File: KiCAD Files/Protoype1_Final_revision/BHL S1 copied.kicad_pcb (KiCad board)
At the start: 4 copper layers, 64 x 64 mm, 108 parts, among them IC1 NUP2105LT1G, IC2 NUP2105LT1G, IC3 IR2136STRPBF, J1 Conn_01x03_Pin, J2 Conn_01x03_Pin, J3 Conn_01x03_Pin, Q1 CSD19502Q5B, Q2 CSD19502Q5B, Q3 CSD19502Q5B, Q4 CSD19502Q5B, Q5 CSD19502Q5B, Q7 CSD19502Q5B, U1 ME6211C30M5, U2 SPX3819M5-L-5-0, U3 Solder Pad, U4 STM32G431CBU6, U5 STM32G431CBU6, Y1 8MHz, Y2 8MHz

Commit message: unlocked files
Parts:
- removed U4: STM32G431CBU6, Footprint for BHL S1:STM32G431CBU6_MCU
- moved R35 3.58 mm to (148.6, 72.8)
- moved R37 3.58 mm to (148.6, 74.5)
- moved Y1 3.58 mm to (144.2, 74.5)
- moved C27 3.56 mm to (134.8, 63.7)
- moved C31 3.56 mm to (134.8, 65.7)
- moved C32 3.56 mm to (134.8, 67.7)
- moved C34 3.56 mm to (134.8, 69.6)
- moved C35 3.56 mm to (134.8, 71.6)
- moved C36 3.56 mm to (134.8, 73.6)
- moved R1 3.56 mm to (138.1, 75.9)
- moved R38 3.56 mm to (138.6, 73.7)
- moved J3 3.56 mm to (138.7, 65.0)
- moved U5 1.94 mm to (145.8, 65.8)

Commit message: Fixed GND Net label issue on PCB creation
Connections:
- AS5600 pad 4: Curr_fdbk1_OPAmp- -> GND
- C1 pad 2: Curr_fdbk1_OPAmp- -> GND
- C11 pad 2: Curr_fdbk1_OPAmp- -> GND
- C12 pad 2: Curr_fdbk1_OPAmp- -> GND
- C14 pad 2: Curr_fdbk1_OPAmp- -> GND
- C16 pad 1: Curr_fdbk1_OPAmp- -> GND
- C18 pad 2: Curr_fdbk1_OPAmp- -> GND
- C2 pad 2: Curr_fdbk1_OPAmp- -> GND
- C22 pad 2: Curr_fdbk1_OPAmp- -> GND
- C23 pad 2: Curr_fdbk1_OPAmp- -> GND
- C24 pad 2: Curr_fdbk1_OPAmp- -> GND
- C25 pad 2: Curr_fdbk1_OPAmp- -> GND
- C26 pad 2: Curr_fdbk1_OPAmp- -> GND
- C27 pad 2: Curr_fdbk1_OPAmp- -> GND
- C28 pad 2: Curr_fdbk1_OPAmp- -> GND
- C29 pad 2: Curr_fdbk1_OPAmp- -> GND
- C3 pad 2: Curr_fdbk1_OPAmp- -> GND
- C30 pad 2: Curr_fdbk1_OPAmp- -> GND
- C31 pad 2: Curr_fdbk1_OPAmp- -> GND
- C32 pad 2: Curr_fdbk1_OPAmp- -> GND
- C33 pad 2: Curr_fdbk1_OPAmp- -> GND
- C34 pad 2: Curr_fdbk1_OPAmp- -> GND
- C35 pad 1: Curr_fdbk1_OPAmp- -> GND
- C36 pad 2: Curr_fdbk1_OPAmp- -> GND
- C4 pad 2: Curr_fdbk1_OPAmp- -> GND
- D1 pad 1: Curr_fdbk1_OPAmp- -> GND
- D2 pad 2: Curr_fdbk1_OPAmp- -> GND
- Header2X2H1 pad 2: Curr_fdbk1_OPAmp- -> GND
- Header2X2H2 pad 2: Curr_fdbk1_OPAmp- -> GND
- IC1 pad 3: Curr_fdbk1_OPAmp- -> GND
- IC2 pad 3: Curr_fdbk1_OPAmp- -> GND
- IC3 pad 10: Curr_fdbk1_OPAmp- -> GND
- IC3 pad 13: Curr_fdbk1_OPAmp- -> GND
- J2 pad 2: Curr_fdbk1_OPAmp- -> GND
- J3 pad 2: Curr_fdbk1_OPAmp- -> GND
- R11 pad 1: Curr_fdbk1_OPAmp- -> GND
- R16 pad 1: Curr_fdbk1_OPAmp- -> GND
- R17 pad 1: Curr_fdbk1_OPAmp- -> GND
- R20 pad 2: Curr_fdbk1_OPAmp- -> GND
- R23 pad 1: Curr_fdbk1_OPAmp- -> GND
- R26 pad 2: Curr_fdbk1_OPAmp- -> GND
- R30 pad 1: Curr_fdbk1_OPAmp- -> GND
- R30 pad 2: Curr_fdbk1_OPAmp- -> GND
- R32 pad 1: Curr_fdbk1_OPAmp- -> GND
- R36 pad 1: Curr_fdbk1_OPAmp- -> GND
- R8 pad 1: Curr_fdbk1_OPAmp- -> GND
- S1 pad 1: Curr_fdbk1_OPAmp- -> GND
- S1 pad 2: Curr_fdbk1_OPAmp- -> GND
- TCAN1051HGVDR1 pad 2: Curr_fdbk1_OPAmp- -> GND
- TCAN1051HGVDR1 pad 8: Curr_fdbk1_OPAmp- -> GND
- U1 pad 2: Curr_fdbk1_OPAmp- -> GND
- U2 pad 2: Curr_fdbk1_OPAmp- -> GND
- U5 pad 11: Curr_fdbk1_OPAmp- -> GND
- U5 pad 13: Curr_fdbk1_OPAmp- -> GND
- U5 pad 19: Curr_fdbk1_OPAmp- -> GND
- U5 pad 49: Curr_fdbk1_OPAmp- -> GND
- Y1 pad 3: Curr_fdbk1_OPAmp- -> GND
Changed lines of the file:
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@@
 			(layers "F.Cu" "F.Mask" "F.Paste")
 			(roundrect_rratio 0.25)
-			(net 20 "Curr_fdbk1_OPAmp-")
+			(net 5 "GND")
 			(pintype "passive")
 		)
@@
 			(layers "F.Cu" "F.Mask" "F.Paste")
 			(roundrect_rratio 0.212766)
-			(net 20 "Curr_fdbk1_OPAmp-")
+			(net 5 "GND")
 			(pintype "passive")
 		)
@@
 			(layers "F.Cu" "F.Mask" "F.Paste")
 			(roundrect_rratio 0.25)
-			(net 20 "Curr_fdbk1_OPAmp-")
+			(net 5 "GND")
 			(pintype "passive")
 		)
@@
 			(layers "F.Cu" "F.Mask" "F.Paste")
 			(roundrect_rratio 0.25)
-			(net 20 "Curr_fdbk1_OPAmp-")
+			(net 5 "GND")
 			(pintype "passive")
 		)
@@
 			(layers "F.Cu" "F.Mask" "F.Paste")
 			(roundrect_rratio 0.25)
-			(net 20 "Curr_fdbk1_OPAmp-")
+			(net 5 "GND")
 			(pintype "passive")
 		)
@@
 			(size 2 4.1)
 			(layers "F.Cu" "F.Mask" "F.Paste")
-			(net 20 "Curr_fdbk1_OPAmp-")
+			(net 5 "GND")
 			(pintype "passive")
 		)
@@
 			(layers "*.Cu" "*.Mask")
 			(remove_unused_layers no)
-			(net 20 "Curr_fdbk1_OPAmp-")
+			(net 5 "GND")
 			(pinfunction "Pin_2")
 			(pintype "passive")
@@
 			(layers "F.Cu" "F.Mask" "F.Paste")
 			(roundrect_rratio 0.25)
-			(net 20 "Curr_fdbk1_OPAmp-")
+			(net 5 "GND")
 			(pintype "passive")
 		)
@@
 			(layers "F.Cu" "F.Mask" "F.Paste")
 			(roundrect_rratio 0.25)
-			(net 20 "Curr_fdbk1_OPAmp-")
+			(net 5 "GND")
 			(pinfunction "V_{SS}")
 			(pintype "power_in")
@@
 			(layers "F.Cu" "F.Mask" "F.Paste")
 			(roundrect_rratio 0.25)
-			(net 20 "Curr_fdbk1_OPAmp-")
+			(net 5 "GND")
 			(pintype "passive")
 		)
@@
 			(layers "F.Cu" "F.Mask" "F.Paste")
 			(roundrect_rratio 0.212766)
-			(net 20 "Curr_fdbk1_OPAmp-")
+			(net 5 "GND")
 			(pintype "passive")
 		)
@@
 			(layers "F.Cu" "F.Mask" "F.Paste")
 			(roundrect_rratio 0.25)
-			(net 20 "Curr_fdbk1_OPAmp-")
+			(net 5 "GND")
 			(pintype "passive")
 		)
@@
 			(layers "F.Cu" "F.Mask" "F.Paste")
 			(roundrect_rratio 0.25)
-			(net 20 "Curr_fdbk1_OPAmp-")
+			(net 5 "GND")
 			(pinfunction "K")
 			(pintype "passive")
@@
 			(layers "F.Cu" "F.Mask" "F.Paste")
 			(roundrect_rratio 0.25)
-			(net 20 "Curr_fdbk1_OPAmp-")
+			(net 5 "GND")
 			(pintype "passive")
 		)
@@
 			(layers "F.Cu" "F.Mask" "F.Paste")
 			(roundrect_rratio 0.25)
-			(net 20 "Curr_fdbk1_OPAmp-")
+			(net 5 "GND")
 			(pinfunction "A")
 			(pintype "passive")
@@
 			(layers "F.Cu" "F.Mask" "F.Paste")
 			(roundrect_rratio 0.25)
-			(net 20 "Curr_fdbk1_OPAmp-")
+			(net 5 "GND")
 			(pintype "passive")
 		)
@@
 			(layers "F.Cu" "F.Mask" "F.Paste")
 			(roundrect_rratio 0.25)
-			(net 20 "Curr_fdbk1_OPAmp-")
+			(net 5 "GND")
 			(pintype "passive")
 		)
@@
 			(layers "F.Cu" "F.Mask" "F.Paste")
 			(roundrect_rratio 0.212766)
-			(net 20 "Curr_fdbk1_OPAmp-")
+			(net 5 "GND")
 			(pintype "passive")
 		)
@@
 			(layers "F.Cu" "F.Mask" "F.Paste")
 			(roundrect_rratio 0.25)
-			(net 20 "Curr_fdbk1_OPAmp-")
+			(net 5 "GND")
 			(pintype "passive")
 		)
@@
 			(layers "F.Cu" "F.Mask" "F.Paste")
 			(roundrect_rratio 0.25)
-			(net 20 "Curr_fdbk1_OPAmp-")
+			(net 5 "GND")
 			(pintype "passive")
 		)
@@
 			(layers "F.Cu" "F.Mask" "F.Paste")
 			(roundrect_rratio 0.25)
-			(net 20 "Curr_fdbk1_OPAmp-")
+			(net 5 "GND")
 			(pintype "passive")
 		)
@@
 			(layers "F.Cu" "F.Mask" "F.Paste")
 			(roundrect_rratio 0.25)
-			(net 20 "Curr_fdbk1_OPAmp-")
+			(net 5 "GND")
 			(pintype "passive")
 		)
@@
 			(size 0.6 1.25)
 			(layers "F.Cu" "F.Mask" "F.Paste")
-			(net 20 "Curr_fdbk1_OPAmp-")
+			(net 5 "GND")
 			(pinfunction "A_3")
 			(pintype "passive")
@@
 			(layers "F.Cu" "F.Mask" "F.Paste")
 			(roundrect_rratio 0.212766)
-			(net 20 "Curr_fdbk1_OPAmp-")
+			(net 5 "GND")
 			(pintype "passive")
 		)
@@
 			(layers "F.Cu" "F.Mask" "F.Paste")
 			(roundrect_rratio 0.25)
-			(net 20 "Curr_fdbk1_OPAmp-")
+			(net 5 "GND")
 			(pinfunction "GND")
 			(pintype "power_in")
@@
 			(layers "F.Cu" "F.Mask" "F.Paste")
 			(roundrect_rratio 0.25)
-			(net 20 "Curr_fdbk1_OPAmp-")
+			(net 5 "GND")
 			(pintype "passive")
 		)
@@
 			(size 1.4 2.1)
 			(layers "F.Cu" "F.Mask" "F.Paste")
-			(net 20 "Curr_fdbk1_OPAmp-")
+			(net 5 "GND")
 			(pintype "passive")
 		)
@@
 			(size 1.4 2.1)
 			(layers "F.Cu" "F.Mask" "F.Paste")
-			(net 20 "Curr_fdbk1_OPAmp-")
+			(net 5 "GND")
 			(pintype "passive")
 		)
@@
 			(layers "F.Cu" "F.Mask" "F.Paste")
 			(roundrect_rratio 0.25)
-			(net 20 "Curr_fdbk1_OPAmp-")
+			(net 5 "GND")
 			(pintype "passive")
 		)
@@
 			(size 0.65 1.925)
 			(layers "F.Cu" "F.Mask" "F.Paste")
-			(net 20 "Curr_fdbk1_OPAmp-")
+			(net 5 "GND")
 			(pinfunction "EN")
 			(pintype "passive")
@@
 			(size 0.65 1.925)
 			(layers "F.Cu" "F.Mask" "F.Paste")
-			(net 20 "Curr_fdbk1_OPAmp-")
+			(net 5 "GND")
 			(pinfunction "COM")
 			(pintype "passive")
@@
 			(size 0.86 0.27)
 			(layers "F.Cu" "F.Paste")
-			(net 20 "Curr_fdbk1_OPAmp-")
+			(net 5 "GND")
 			(pinfunction "PA3")
 			(pintype "bidirectional")
@@
 			(size 0.27 0.86)
 			(layers "F.Cu" "F.Paste")
-			(net 20 "Curr_fdbk1_OPAmp-")
+			(net 5 "GND")
 			(pinfunction "PA5")
 			(pintype "bidirectional")
@@
 			(size 0.27 0.86)
 			(layers "F.Cu" "F.Paste")
-			(net 20 "Curr_fdbk1_OPAmp-")
+			(net 5 "GND")
 			(pinfunction "PB2")
 			(pintype "bidirectional")
@@
 			(size 5.6 5.6)
 			(layers "F.Cu")
-			(net 20 "Curr_fdbk1_OPAmp-")
+			(net 5 "GND")
 			(pinfunction "VSS")
 			(pintype "power_in")
@@
 			(layers "*.Cu" "*.Mask")
 			(remove_unused_layers no)
-			(net 20 "Curr_fdbk1_OPAmp-")
+			(net 5 "GND")
 			(pinfunction "2")
 			(pintype "input")
@@
 			(layers "F.Cu" "F.Mask" "F.Paste")
 			(roundrect_rratio 0.25)
-			(net 20 "Curr_fdbk1_OPAmp-")
+			(net 5 "GND")
 			(pintype "passive")
 		)
@@
 			(layers "F.Cu" "F.Mask" "F.Paste")
 			(roundrect_rratio 0.25)
-			(net 20 "Curr_fdbk1_OPAmp-")
+			(net 5 "GND")
 			(pintype "passive")
 		)
@@
 			(size 0.65 1.528)
 			(layers "F.Cu" "F.Mask" "F.Paste")
-			(net 20 "Curr_fdbk1_OPAmp-")
+			(net 5 "GND")
 			(pinfunction "GND")
 			(pintype "power_in")
@@
 			(size 0.65 1.528)
 			(layers "F.Cu" "F.Mask" "F.Paste")
-			(net 20 "Curr_fdbk1_OPAmp-")
+			(net 5 "GND")
 			(pinfunction "STB")
 			(pintype "power_in")
@@
 			(layers "F.Cu" "F.Mask" "F.Paste")
 			(roundrect_rratio 0.212766)
-			(net 20 "Curr_fdbk1_OPAmp-")
+			(net 5 "GND")
 			(pintype "passive")
 		)
@@
 			(layers "F.Cu" "F.Mask" "F.Paste")
 			(roundrect_rratio 0.25)
-			(net 20 "Curr_fdbk1_OPAmp-")
+			(net 5 "GND")
 			(pintype "passive")
 		)
@@
 			(layers "F.Cu" "F.Mask" "F.Paste")
 			(roundrect_rratio 0.25)
-			(net 20 "Curr_fdbk1_OPAmp-")
+			(net 5 "GND")
 			(pintype "passive")
 		)
@@
 			(layers "*.Cu" "*.Mask")
 			(remove_unused_layers no)
-			(net 20 "Curr_fdbk1_OPAmp-")
+			(net 5 "GND")
 			(pinfunction "2")
 			(pintype "input")
@@
 			(layers "F.Cu" "F.Mask" "F.Paste")
 			(roundrect_rratio 0.212766)
-			(net 20 "Curr_fdbk1_OPAmp-")
+			(net 5 "GND")
 			(pintype "passive")
 		)
@@
 			(layers "F.Cu" "F.Mask" "F.Paste")
 			(roundrect_rratio 0.25)
-			(net 20 "Curr_fdbk1_OPAmp-")
+			(net 5 "GND")
 			(pintype "passive")
 		)
@@
 			(layers "F.Cu" "F.Mask" "F.Paste")
 			(roundrect_rratio 0.25)
-			(net 20 "Curr_fdbk1_OPAmp-")
+			(net 5 "GND")
 			(pintype "passive")
 		)
@@
 			(layers "F.Cu" "F.Mask" "F.Paste")
 			(roundrect_rratio 0.212766)
-			(net 20 "Curr_fdbk1_OPAmp-")
+			(net 5 "GND")
 			(pintype "passive")
 		)
@@
 			(layers "F.Cu" "F.Mask" "F.Paste")
 			(roundrect_rratio 0.25)
-			(net 20 "Curr_fdbk1_OPAmp-")
+			(net 5 "GND")
 			(pintype "passive")
 		)
@@
 			(size 0.6 1.25)
 			(layers "F.Cu" "F.Mask" "F.Paste")
-			(net 20 "Curr_fdbk1_OPAmp-")
+			(net 5 "GND")
 			(pinfunction "A_3")
 			(pintype "passive")
@@
 			(layers "F.Cu" "F.Mask" "F.Paste")
 			(roundrect_rratio 0.212766)
-			(net 20 "Curr_fdbk1_OPAmp-")
+			(net 5 "GND")
 			(pintype "passive")
 		)
@@
 			(layers "*.Cu" "*.Mask")
 			(remove_unused_layers no)
-			(net 20 "Curr_fdbk1_OPAmp-")
+			(net 5 "GND")
 			(pinfunction "Pin_2")
 			(pintype "passive")
@@
 			(layers "F.Cu" "F.Mask" "F.Paste")
 			(roundrect_rratio 0.25)
-			(net 20 "Curr_fdbk1_OPAmp-")
+			(net 5 "GND")
 			(pintype "passive")
 		)
@@
 			(layers "F.Cu" "F.Mask" "F.Paste")
 			(roundrect_rratio 0.25)
-			(net 20 "Curr_fdbk1_OPAmp-")
+			(net 5 "GND")
 			(pintype "passive")
 		)
@@
 			(size 0.4 1.9)
 			(layers "F.Cu" "F.Mask" "F.Paste")
-			(net 20 "Curr_fdbk1_OPAmp-")
+			(net 5 "GND")
 			(pinfunction "3")
 			(pintype "passive")
@@
 			(layers "F.Cu" "F.Mask" "F.Paste")
 			(roundrect_rratio 0.25)
-			(net 20 "Curr_fdbk1_OPAmp-")
+			(net 5 "GND")
 			(pintype "passive")
 		)
@@
 			(size 0.65 1.5)
 			(layers "B.Cu" "B.Mask" "B.Paste")
-			(net 20 "Curr_fdbk1_OPAmp-")
+			(net 5 "GND")
 			(pinfunction "GND")
 			(pintype "power_in")

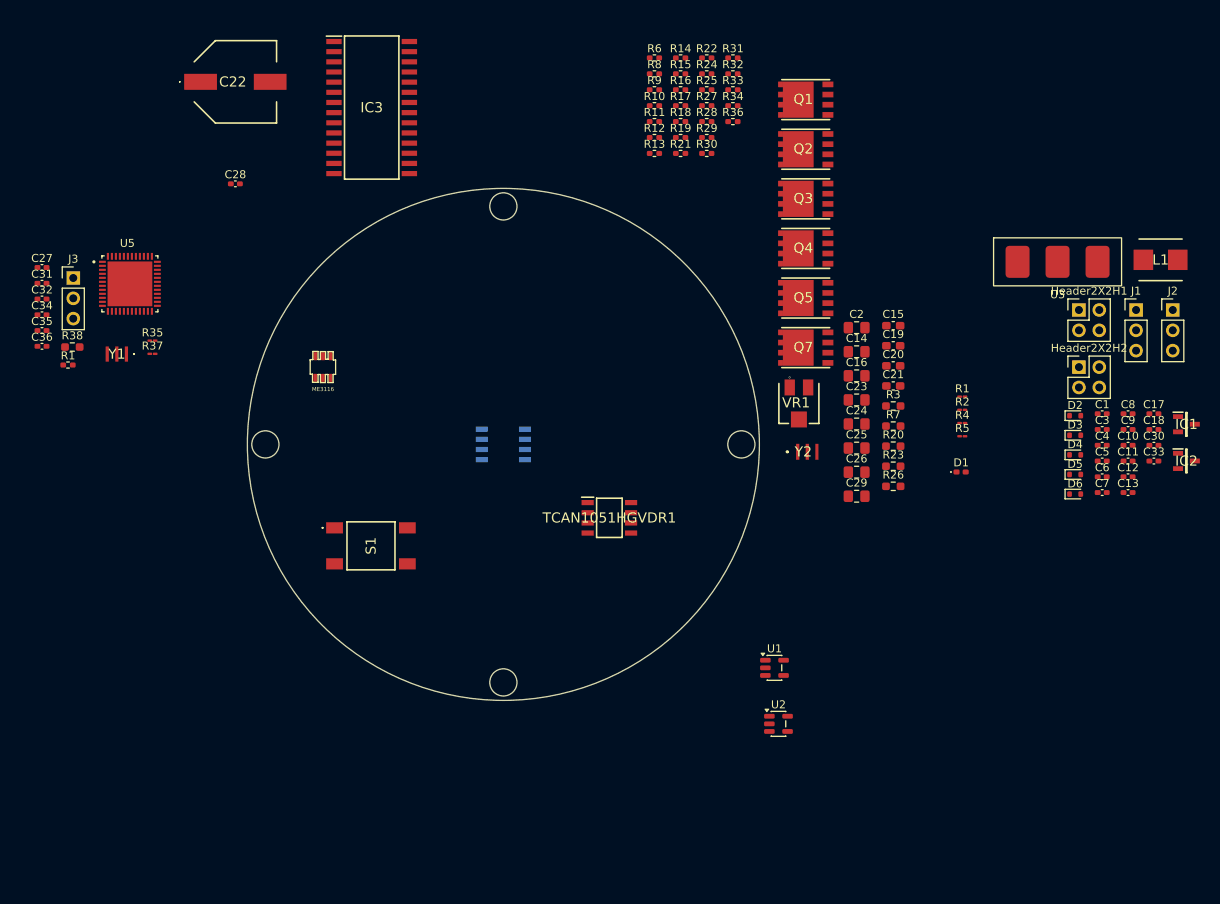
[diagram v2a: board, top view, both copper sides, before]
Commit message: Terminator block added, footprint error fixed, 9 schematic errors remains, may need to update all file paths of the symbol library.
Moo
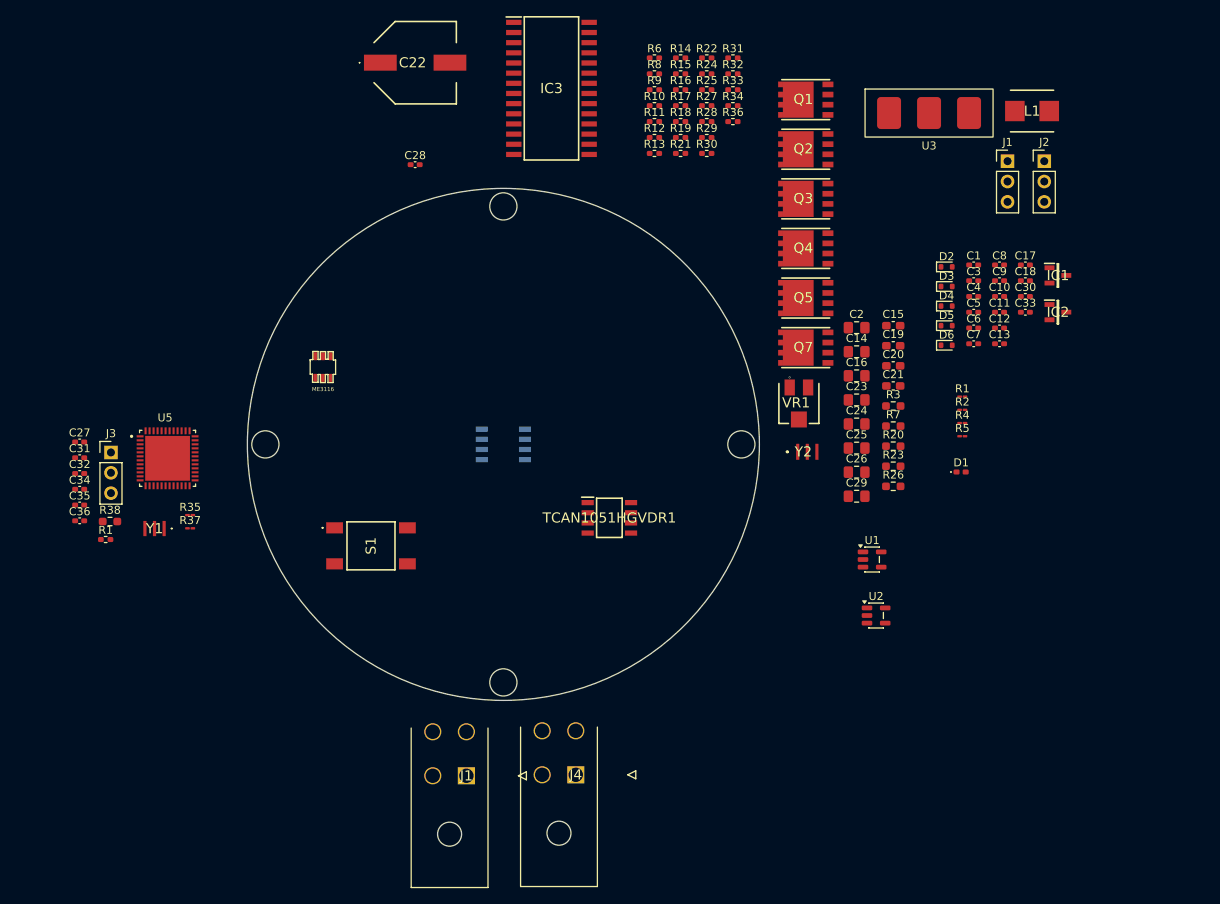
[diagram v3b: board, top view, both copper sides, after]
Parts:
- removed Header2X2H1, Header2X2H2: ~, Connector_PinHeader_2.54mm:PinHeader_2x02_P2.54mm_Vertical
- added J1: 39-30-1042, Footprint for BHL S1:Terminator, F.Cu at (187.9, 127.2)
- added J4: 39-30-1042, Footprint for BHL S1:Terminator, F.Cu at (201.6, 127.1)
- moved C4 24.6 mm to (251.3, 67.3)
- moved C5 24.6 mm to (251.3, 69.3)
- moved C6 24.6 mm to (251.3, 71.3)
- moved C7 24.6 mm to (251.3, 73.2)
- moved D3 24.6 mm to (247.9, 66.1)
- moved D2 24.6 mm to (247.9, 63.6)
- moved C1 24.6 mm to (251.3, 63.4)
- moved C3 24.6 mm to (251.3, 65.4)
- moved D4 24.6 mm to (247.9, 68.5)
- moved D5 24.6 mm to (247.9, 71.0)
- moved D6 24.6 mm to (247.9, 73.4)
- moved C30 24.6 mm to (257.8, 67.3)
- moved C33 24.6 mm to (257.8, 69.3)
- moved L1 24.6 mm to (258.6, 44.1)
- moved C17 24.6 mm to (257.8, 63.4)
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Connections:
- ME3116 pad 1: (no net) -> Net-(ME3116-BS)
- ME3116 pad 2: (no net) -> GND
- ME3116 pad 3: (no net) -> Net-(ME3116-FB)
- ME3116 pad 4: (no net) -> Net-(ME3116-EN)
- ME3116 pad 5: (no net) -> Net-(D3-K)
- ME3116 pad 6: (no net) -> Net-(D2-K)

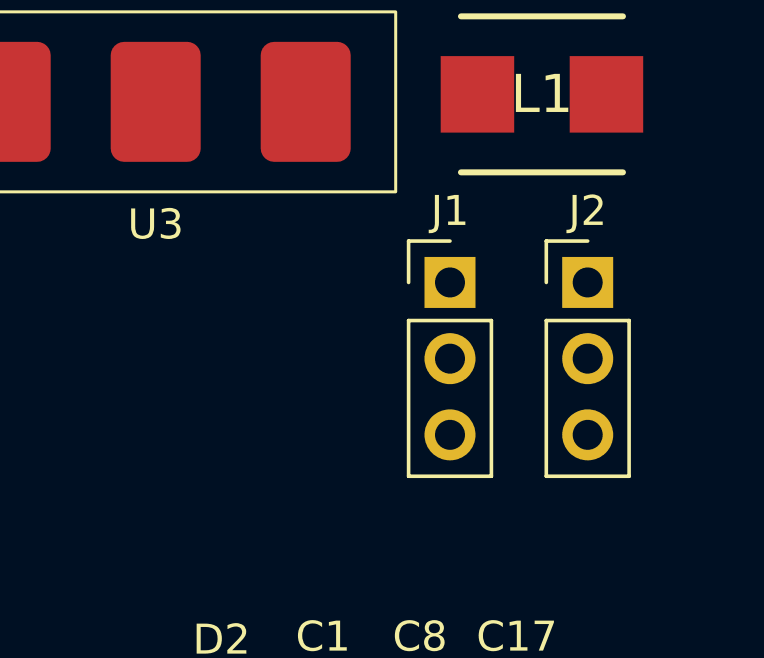
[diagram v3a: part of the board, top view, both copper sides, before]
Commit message: Pin header duplicated fixed
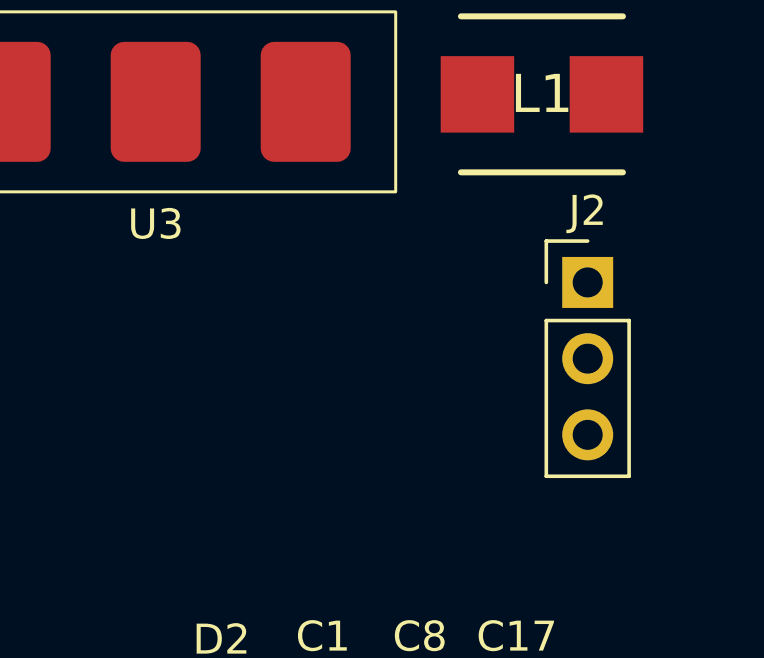
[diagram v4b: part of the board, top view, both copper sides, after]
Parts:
- removed the J1 at (255.5, 50.4)
